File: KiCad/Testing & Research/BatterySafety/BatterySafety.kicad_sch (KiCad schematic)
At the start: 14 parts

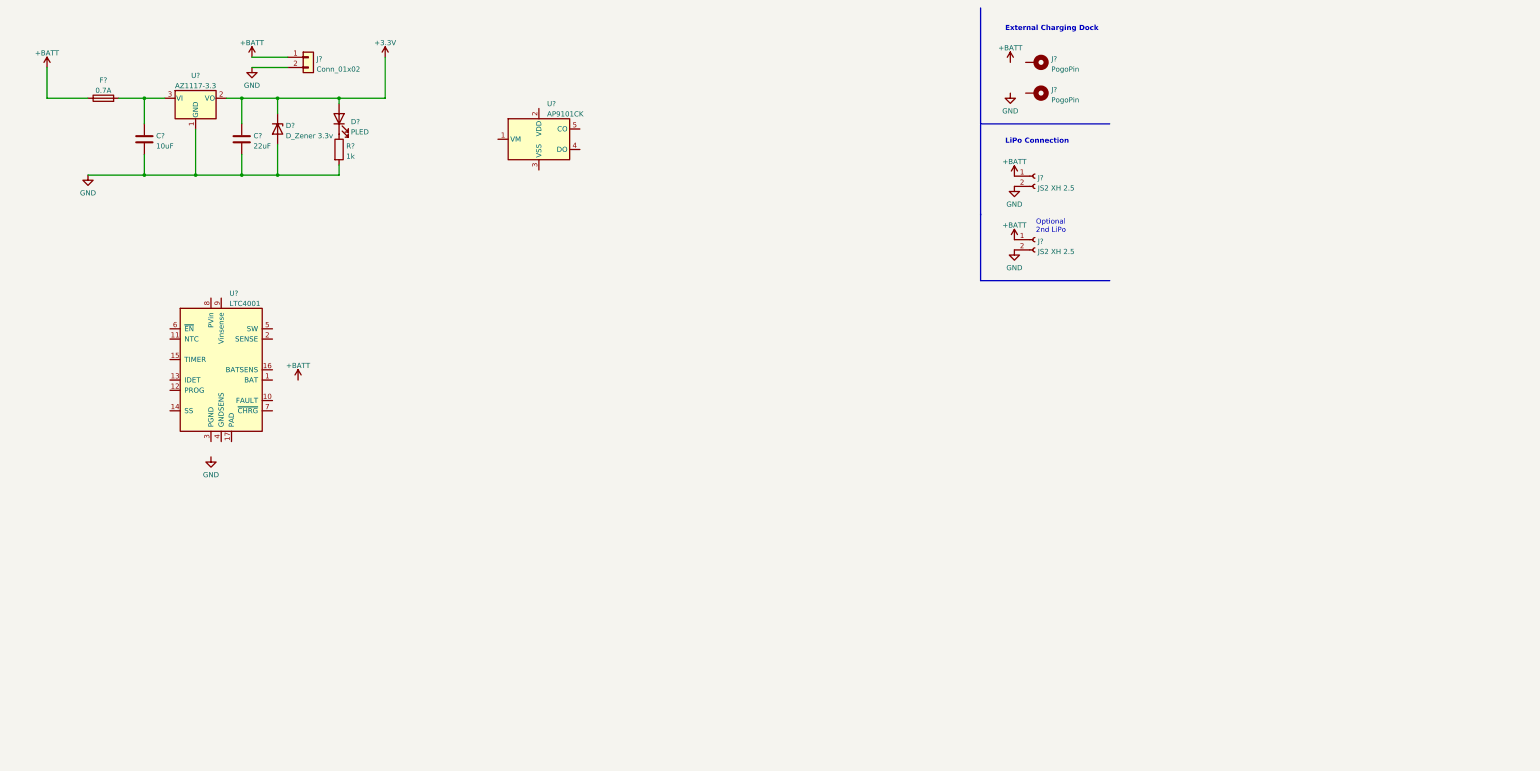
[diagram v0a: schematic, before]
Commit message: Implemented basic battery circuit
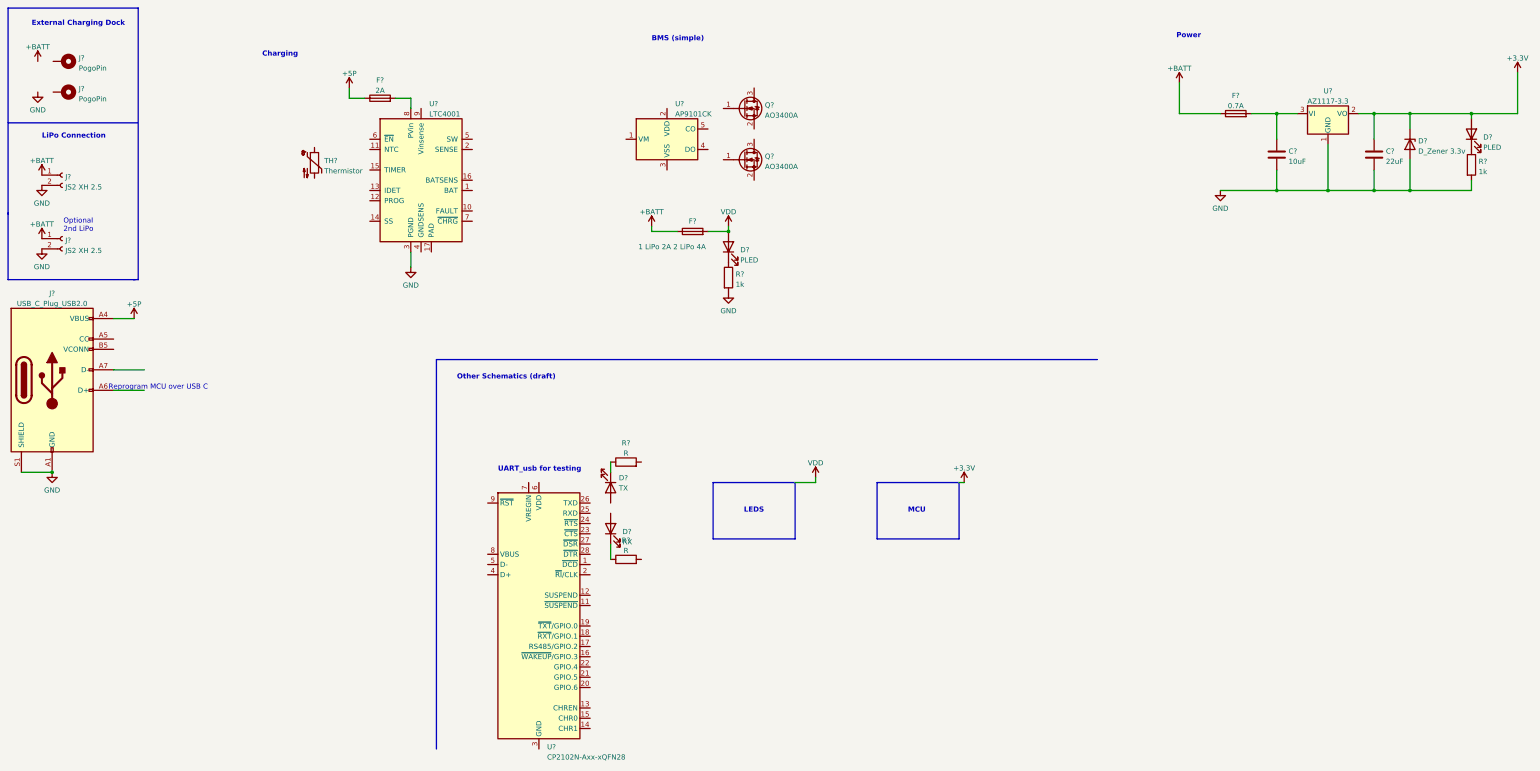
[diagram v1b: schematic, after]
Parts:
- removed J?: Conn_01x02, symbol Connector_Generic:Conn_01x02
- added D?: RX, symbol Device:LED
- added D?: TX, symbol Device:LED
- added D?: PLED, symbol Device:LED
- added F?: 2A, symbol Device:Fuse
- added F?: 1 LiPo 2A 2 LiPo 4A, symbol Device:Fuse
- added J?: USB_C_Plug_USB2.0, symbol Connector:USB_C_Plug_USB2.0
- added Q? (x2): AO3400A, Package_TO_SOT_SMD:SOT-23, symbol Transistor_FET:AO3400A
- added R? (x2): R, symbol Device:R
- added R?: 1k, symbol Device:R
- added TH?: Thermistor, symbol Device:Thermistor_NTC
- added U?: CP2102N-Axx-xQFN28, Package_DFN_QFN:QFN-28-1EP_5x5mm_P0.5mm_EP3.35x3.35mm, symbol Interface_USB:CP2102N-Axx-xQFN28
- J? (x2): Link (none) -> https://www.digikey.be/nl/products/detail/mill-max-manufact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; MPN (none) -> 0921-1-15-20-75-14-11-0
- U?: Link (none) -> https://www.digikey.be/nl/products/detail/analog-devices-in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; MPN (none) -> LTC4001EUF#TRPBF
- U?: Link (none) -> https://www.digikey.be/nl/products/detail/diodes-incorporat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; MPN (none) -> AP9101CK6-ANTRG1
- U?: Link (none) -> digikey.be/nl/products/detail/diodes-incorporated/AZ1117IH-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; MPN (none) -> AZ1117IH-5.0TRG1
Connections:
- net +BATT: now also F?.1
- net GND: now also U?.3 (PGND), J?.A1 (GND), J?.A12 (GND), J?.B1 (GND), J?.B12 (GND), J?.S1 (SHIELD), R?.2
- net at U?.8 (PVin): now also F?.2
- new net: D?.1 (K), R?.1 (x3)
- new net: U?.29 (GND), U?.3 (GND)
- new net +5P: F?.1, J?.A4 (VBUS), J?.A9 (VBUS), J?.B4 (VBUS), J?.B9 (VBUS)
- new net VDD: D?.2 (A), F?.2
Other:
- note added: "BMS (simple)"
- note added: "Charging"
- note added: "LEDS"
- note added: "MCU"
- note added: "Other Schematics (draft)"
- note added: "Power"
- note added: "Reprogram MCU over USB C"
- note added: "UART_usb for testing"
- moved on the sheet: C?, D?, F?, J?, R?, U?
